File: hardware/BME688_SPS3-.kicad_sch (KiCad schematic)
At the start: 10 parts, among them U59 USBLC6-2P6, U6 BME688

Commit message: Debugging LED added
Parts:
- R3, R4, R5, R6: footprint Resistor_SMD:R_0603_1608Metric -> Resistor_SMD:R_0805_2012Metric
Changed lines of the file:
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@@
 			)
 		)
-		(property "Footprint" "Resistor_SMD:R_0603_1608Metric"
+		(property "Footprint" "Resistor_SMD:R_0805_2012Metric"
 			(at 172.212 104.14 90)
 			(effects
@@
 			)
 		)
-		(property "Footprint" "Resistor_SMD:R_0603_1608Metric"
+		(property "Footprint" "Resistor_SMD:R_0805_2012Metric"
 			(at 181.102 104.14 90)
 			(effects
@@
 			)
 		)
-		(property "Footprint" "Resistor_SMD:R_0603_1608Metric"
+		(property "Footprint" "Resistor_SMD:R_0805_2012Metric"
 			(at 84.328 101.6 90)
 			(effects
@@
 			)
 		)
-		(property "Footprint" "Resistor_SMD:R_0603_1608Metric"
+		(property "Footprint" "Resistor_SMD:R_0805_2012Metric"
 			(at 120.142 95.25 90)
 			(effects

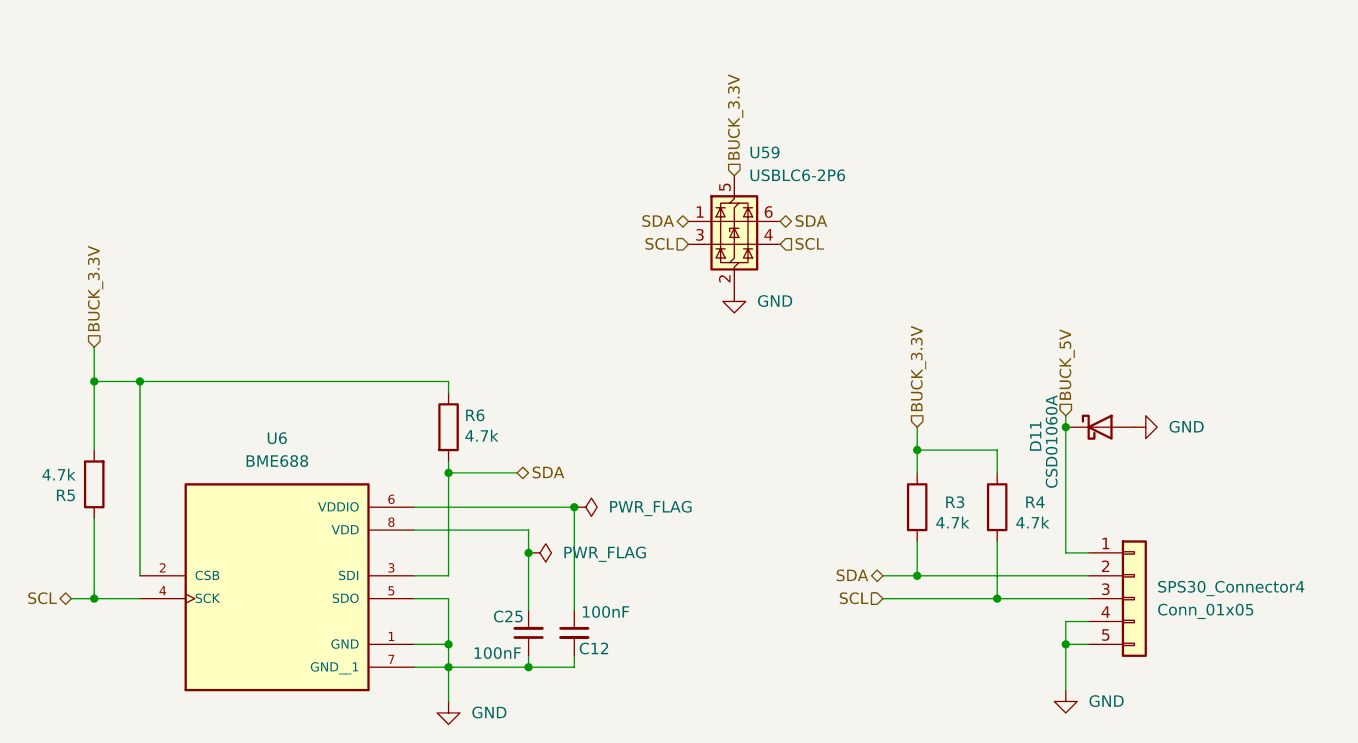
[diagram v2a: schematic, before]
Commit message: Unified I2C pull-ups to MCU page
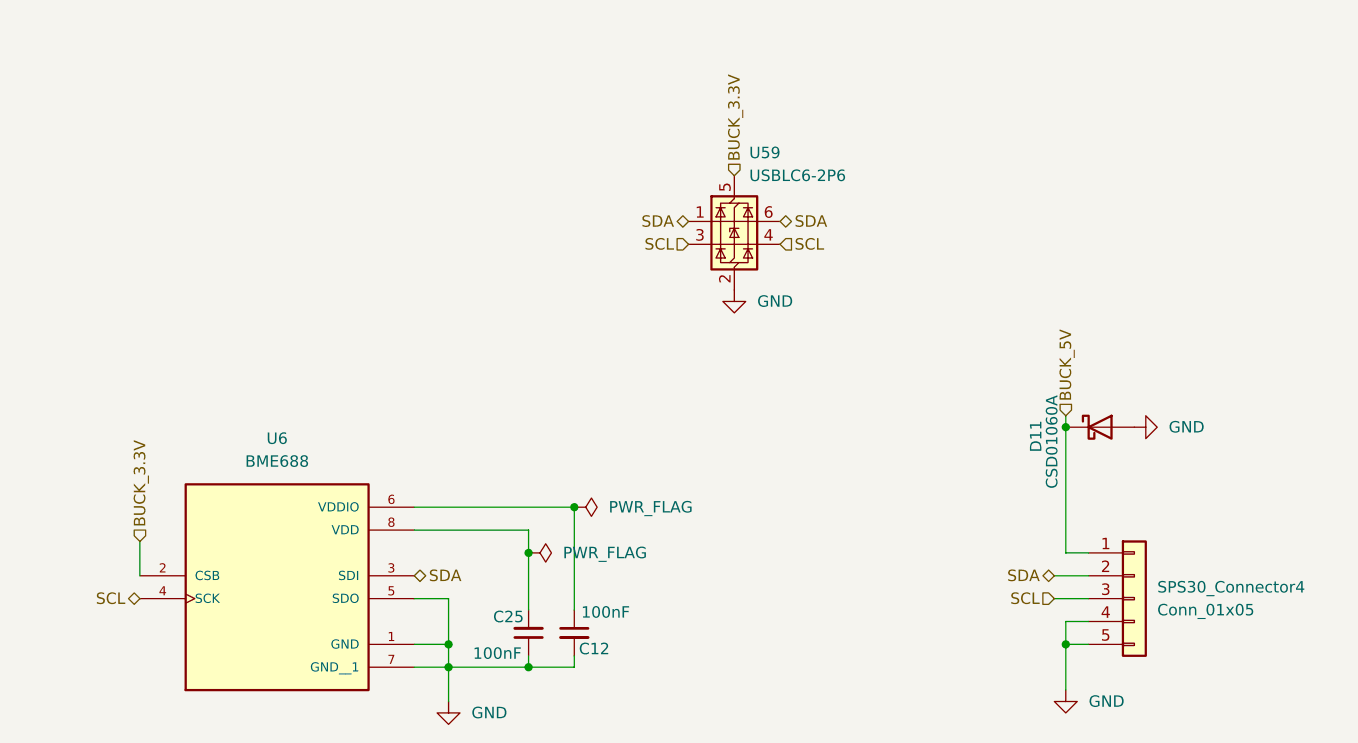
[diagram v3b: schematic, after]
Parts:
- removed R3, R4, R5, R6: 4.7k, Resistor_SMD:R_0805_2012Metric, symbol Device:R

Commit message: Fixed MCU JTAG/Reordered pages
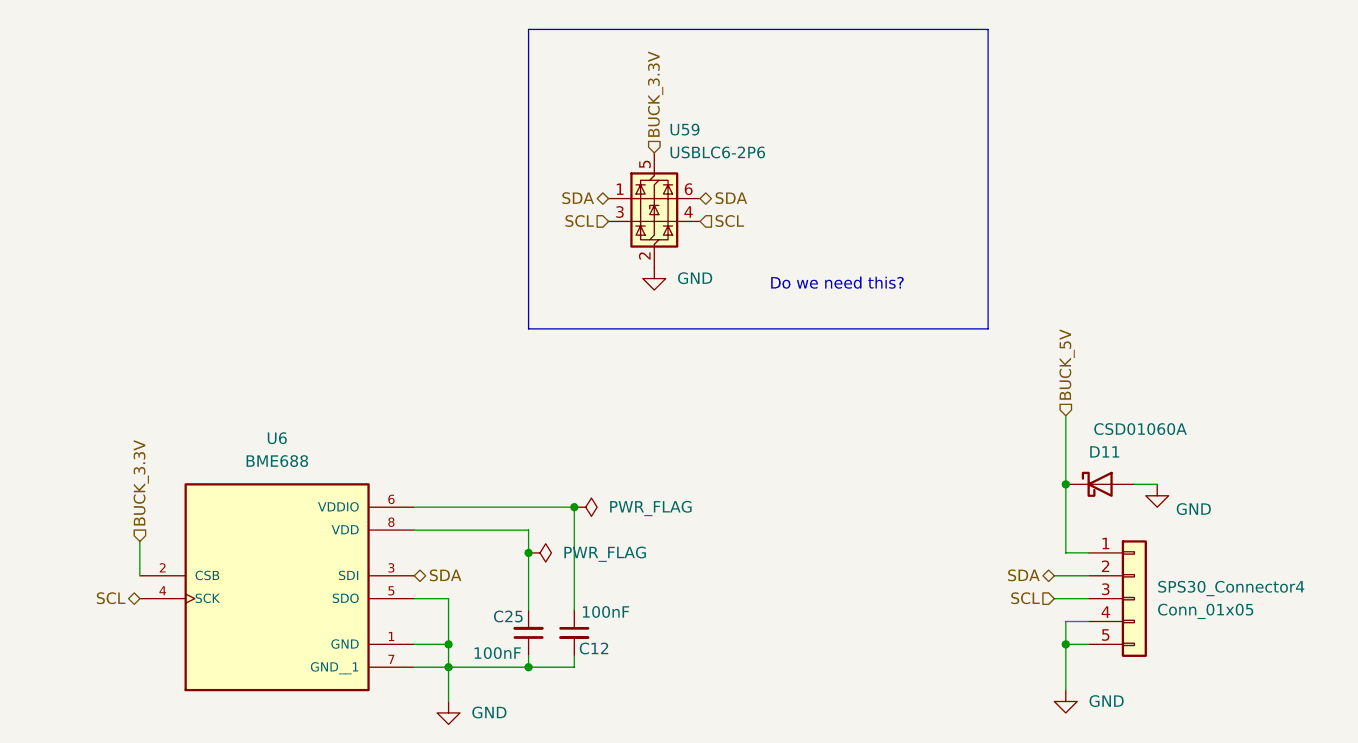
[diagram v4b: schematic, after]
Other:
- note added: "Do we need this?"
- moved on the sheet: D11, U59
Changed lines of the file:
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@@
 	(generator_version "9.0")
 	(paper "A4")
+	(rectangle
+		(start 130.81 51.054)
+		(end 181.864 84.328)
+		(stroke
+			(width 0)
+			(type default)
+		)
+		(fill
+			(type none)
+		)
+	)
+	(text "Do we need this?"
+		(exclude_from_sim no)
+		(at 165.1 79.502 0)
+		(effects
+			(font
+				(size 1.27 1.27)
+				(color 255 0 0 1)
+			)
+		)
+	)
 	(junction
 		(at 135.89 104.14)
@@
 	)
 	(junction
-		(at 190.5 95.25)
-		(diameter 0)
-		(color 0 0 0 0)
-	)
-	(junction
 		(at 121.92 121.92)
 		(diameter 0)
@@
 	)
 	(junction
+		(at 190.5 101.6)
+		(diameter 0)
+		(color 0 0 0 0)
+	)
+	(junction
 		(at 130.81 109.22)
 		(diameter 0)
@@
 	(wire
 		(pts
+			(xy 198.12 101.6) (xy 200.66 101.6)
+		)
+		(stroke
+			(width 0)
+			(type default)
+		)
+	)
+	(wire
+		(pts
 			(xy 135.89 120.65) (xy 135.89 121.92)
 		)
@@
 	(wire
 		(pts
-			(xy 190.5 93.98) (xy 190.5 95.25)
-		)
-		(stroke
-			(width 0)
-			(type default)
-		)
-	)
-	(wire
-		(pts
 			(xy 190.5 116.84) (xy 190.5 119.38)
 		)
@@
 	(wire
 		(pts
+			(xy 190.5 93.98) (xy 190.5 101.6)
+		)
+		(stroke
+			(width 0)
+			(type default)
+		)
+	)
+	(wire
+		(pts
 			(xy 118.11 114.3) (xy 121.92 114.3)
 		)
@@
 	(wire
 		(pts
-			(xy 190.5 95.25) (xy 190.5 109.22)
-		)
-		(stroke
-			(width 0)
-			(type default)
-		)
-	)
-	(wire
-		(pts
 			(xy 189.23 114.3) (xy 193.04 114.3)
 		)
@@
 		(pts
 			(xy 118.11 121.92) (xy 121.92 121.92)
+		)
+		(stroke
+			(width 0)
+			(type default)
+		)
+	)
+	(wire
+		(pts
+			(xy 190.5 101.6) (xy 190.5 109.22)
 		)
 		(stroke
@@
 	(hierarchical_label "SDA"
 		(shape bidirectional)
-		(at 148.59 72.39 180)
+		(at 139.7 69.85 180)
 		(effects
 			(font
@@
 	(hierarchical_label "BUCK_3.3V"
 		(shape input)
-		(at 153.67 67.31 90)
+		(at 144.78 64.77 90)
 		(effects
 			(font
@@
 	(hierarchical_label "SCL"
 		(shape input)
-		(at 148.59 74.93 180)
+		(at 139.7 72.39 180)
 		(effects
 			(font
@@
 	(hierarchical_label "SDA"
 		(shape bidirectional)
-		(at 158.75 72.39 0)
+		(at 149.86 69.85 0)
 		(effects
 			(font
@@
 	(hierarchical_label "SCL"
 		(shape input)
-		(at 158.75 74.93 0)
+		(at 149.86 72.39 0)
 		(effects
 			(font
@@
 	(symbol
 		(lib_id "Power_Protection:USBLC6-2P6")
-		(at 153.67 72.39 0)
+		(at 144.78 69.85 0)
 		(unit 1)
 		(exclude_from_sim no)
@@
 		(fields_autoplaced yes)
 		(property "Reference" "U59"
-			(at 155.3211 64.77 0)
+			(at 146.4311 62.23 0)
 			(effects
 				(font
@@
 		)
 		(property "Value" "USBLC6-2P6"
-			(at 155.3211 67.31 0)
+			(at 146.4311 64.77 0)
 			(effects
 				(font
@@
 		)
 		(property "Footprint" "Package_TO_SOT_SMD:SOT-666"
-			(at 154.686 79.121 0)
+			(at 145.796 76.581 0)
 			(effects
 				(font
@@
 		)
 		(property "Datasheet" "https://www.st.com/resource/en/datasheet/usblc6-2.pdf"
-			(at 154.686 81.026 0)
+			(at 145.796 78.486 0)
 			(effects
 				(font
@@
 		)
 		(property "Description" "Very low capacitance ESD protection diode, 2 data-line, SOT-666"
-			(at 153.67 72.39 0)
+			(at 144.78 69.85 0)
 			(effects
 				(font
@@
 	(symbol
 		(lib_id "Diode:CSD01060A")
-		(at 194.31 95.25 0)
+		(at 194.31 101.6 0)
 		(unit 1)
 		(exclude_from_sim no)
@@
 		(dnp no)
 		(property "Reference" "D11"
-			(at 187.198 94.488 90)
+			(at 196.596 98.044 0)
 			(effects
 				(font
@@
 		)
 		(property "Value" "CSD01060A"
-			(at 188.976 91.694 90)
+			(at 203.962 95.504 0)
 			(effects
 				(font
@@
 		)
 		(property "Footprint" "Package_TO_SOT_THT:TO-220-2_Vertical"
-			(at 194.31 99.695 0)
+			(at 194.31 106.045 0)
 			(effects
 				(font
@@
 		)
 		(property "Datasheet" "https://www.wolfspeed.com/media/downloads/87/CSD01060.pdf"
-			(at 194.31 95.25 0)
+			(at 194.31 101.6 0)
 			(effects
 				(font
@@
 		)
 		(property "Description" "600V, 1A, SiC Schottky Diode, TO-220"
-			(at 194.31 95.25 0)
+			(at 194.31 101.6 0)
 			(effects
 				(font
@@
 	(symbol
 		(lib_id "power:GND")
-		(at 198.12 95.25 90)
+		(at 200.66 101.6 0)
 		(unit 1)
 		(exclude_from_sim no)
@@
 		(on_board yes)
 		(dnp no)
-		(fields_autoplaced yes)
 		(property "Reference" "#PWR0116"
-			(at 204.47 95.25 0)
+			(at 200.66 107.95 0)
 			(effects
 				(font
@@
 		)
 		(property "Value" "GND"
-			(at 201.93 95.2499 90)
-			(effects
-				(font
-					(size 1.27 1.27)
-				)
-				(justify right)
+			(at 204.724 104.394 0)
+			(effects
+				(font
+					(size 1.27 1.27)
+				)
 			)
 		)
 		(property "Footprint" ""
-			(at 198.12 95.25 0)
+			(at 200.66 101.6 0)
 			(effects
 				(font
@@
 		)
 		(property "Datasheet" ""
-			(at 198.12 95.25 0)
+			(at 200.66 101.6 0)
 			(effects
 				(font
@@
 		)
 		(property "Description" "Power symbol creates a global label with name \"GND\" , ground"
-			(at 198.12 95.25 0)
+			(at 200.66 101.6 0)
 			(effects
 				(font
@@
 	(symbol
 		(lib_id "power:GND")
-		(at 153.67 80.01 0)
+		(at 144.78 77.47 0)
 		(unit 1)
 		(exclude_from_sim no)
@@
 		(fields_autoplaced yes)
 		(property "Reference" "#PWR0114"
-			(at 153.67 86.36 0)
+			(at 144.78 83.82 0)
 			(effects
 				(font
@@
 		)
 		(property "Value" "GND"
-			(at 156.21 81.2799 0)
+			(at 147.32 78.7399 0)
 			(effects
 				(font
@@
 		)
 		(property "Footprint" ""
-			(at 153.67 80.01 0)
+			(at 144.78 77.47 0)
 			(effects
 				(font
@@
 		)
 		(property "Datasheet" ""
-			(at 153.67 80.01 0)
+			(at 144.78 77.47 0)
 			(effects
 				(font
@@
 		)
 		(property "Description" "Power symbol creates a global label with name \"GND\" , ground"
-			(at 153.67 80.01 0)
-			(effects
-				(font
+			(at 144.78 77.47 0)
+			(effects
+				(font

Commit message: Replaced 3.3V symbol
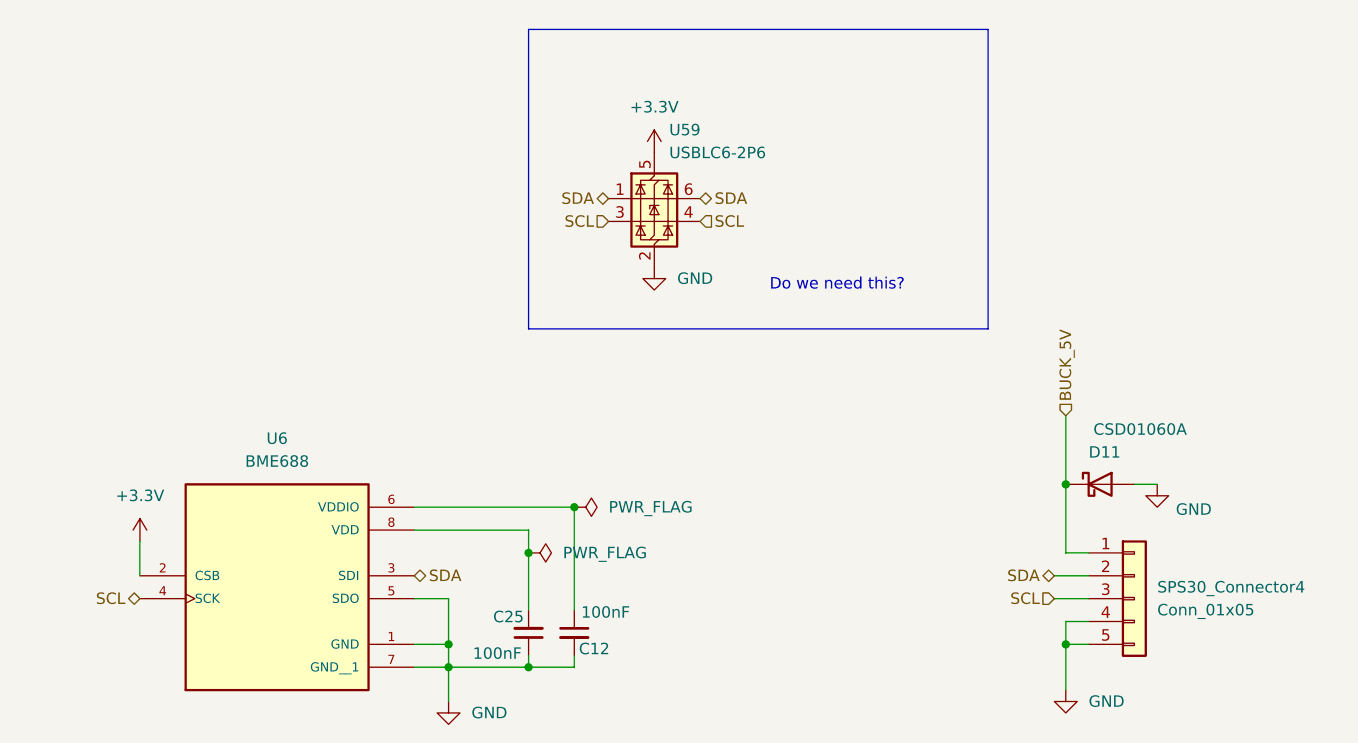
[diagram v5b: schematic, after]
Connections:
- net BUCK_3.3V renamed +3.3V
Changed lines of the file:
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@@
-		)
-	)
-	(hierarchical_label "BUCK_3.3V"
-		(shape input)
-		(at 144.78 64.77 90)
-		(effects
-			(font
-				(size 1.27 1.27)
-			)
-			(justify left)
 		)
 	)
@@
 		(shape bidirectional)
 		(at 149.86 69.85 0)
-		(effects
-			(font
-				(size 1.27 1.27)
-			)
-			(justify left)
-		)
-	)
-	(hierarchical_label "BUCK_3.3V"
-		(shape input)
-		(at 87.63 107.95 90)
 		(effects
 			(font
@@
 	)
 	(symbol
+		(lib_id "power:+3.3V")
+		(at 87.63 107.95 0)
+		(unit 1)
+		(exclude_from_sim no)
+		(in_bom yes)
+		(on_board yes)
+		(dnp no)
+		(fields_autoplaced yes)
+		(property "Reference" "#PWR077"
+			(at 87.63 111.76 0)
+			(effects
+				(font
+					(size 1.27 1.27)
+				)
+				(hide yes)
+			)
+		)
+		(property "Value" "+3.3V"
+			(at 87.63 102.87 0)
+			(effects
+				(font
+					(size 1.27 1.27)
+				)
+			)
+		)
+		(property "Footprint" ""
+			(at 87.63 107.95 0)
+			(effects
+				(font
+					(size 1.27 1.27)
+				)
+				(hide yes)
+			)
+		)
+		(property "Datasheet" ""
+			(at 87.63 107.95 0)
+			(effects
+				(font
+					(size 1.27 1.27)
+				)
+				(hide yes)
+			)
+		)
+		(property "Description" "Power symbol creates a global label with name \"+3.3V\""
+			(at 87.63 107.95 0)
+			(effects
+				(font
+					(size 1.27 1.27)
+				)
+				(hide yes)
+			)
+		)
+		(pin "1"
+		)
+		(instances
+			(project "Senior_Design"
+				(path "/8f5928e8-0fc1-4443-a20f-3bfeb956761e/140ad835-eaa4-4a8c-a4e7-0525bbf22a2e"
+					(reference "#PWR077")
+					(unit 1)
+				)
+			)
+		)
+	)
+	(symbol
 		(lib_id "Device:C_Small")
 		(at 135.89 118.11 0)
@@
 					(unit 1)
 				)
+			)
+		)
+	)
+	(symbol
+		(lib_id "power:+3.3V")
+		(at 144.78 64.77 0)
+		(unit 1)
+		(exclude_from_sim no)
+		(in_bom yes)
+		(on_board yes)
+		(dnp no)
+		(fields_autoplaced yes)
+		(property "Reference" "#PWR078"
+			(at 144.78 68.58 0)
+			(effects
+				(font
+					(size 1.27 1.27)
+				)
+				(hide yes)
+			)
+		)
+		(property "Value" "+3.3V"
+			(at 144.78 59.69 0)
+			(effects
+				(font
+					(size 1.27 1.27)
+				)
+			)
+		)
+		(property "Footprint" ""
+			(at 144.78 64.77 0)
+			(effects
+				(font
+					(size 1.27 1.27)
+				)
+				(hide yes)
+			)
+		)
+		(property "Datasheet" ""
+			(at 144.78 64.77 0)
+			(effects
+				(font
+					(size 1.27 1.27)
+				)
+				(hide yes)
+			)
+		)
+		(property "Description" "Power symbol creates a global label with name \"+3.3V\""
+			(at 144.78 64.77 0)
+			(effects
+				(font
+					(size 1.27 1.27)
+				)
+				(hide yes)
+			)
+		)
+		(pin "1"
+		)
+		(instances
+			(project "Senior_Design"
+				(path "/8f5928e8-0fc1-4443-a20f-3bfeb956761e/140ad835-eaa4-4a8c-a4e7-0525bbf22a2e"
+					(reference "#PWR078")
+					(unit 1)
+				)

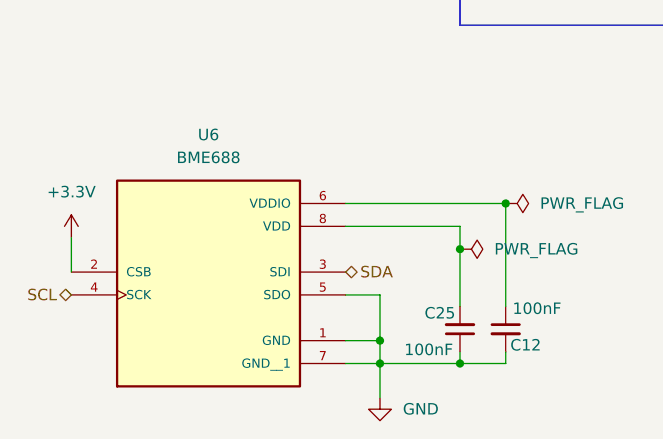
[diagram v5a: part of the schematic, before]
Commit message: updated major symbol and footprints
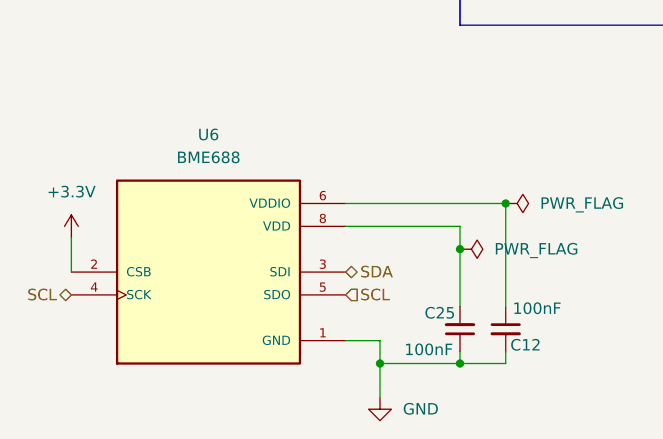
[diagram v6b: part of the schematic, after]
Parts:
- U6: footprint Custom_Parts:IC_BME688 -> pyronet_footprints:IC_BME688; symbol BME688:BME688 -> pyronet_symbols:BME688; Availability (none) -> In Stock; Check_prices (none) -> https://www.snapeda.com/parts/BME688/Bosch/view-part/?ref=e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; Description_1 (none) -> Gas sensor measuring relative humidity, barometric pressure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; MF (none) -> Bosch Sensortec; MP (none) -> BME688; Package (none) -> None; Price (none) -> None; Purchase-URL (none) -> https://www.snapeda.com/api/url_track_click_mouser/?unipart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; SnapEDA_Link (none) -> https://www.snapeda.com/parts/BME688/Bosch/view-part/?ref=s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
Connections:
- net GND: no longer U6.5 (SDO)
- net SCL: now also U6.5 (SDO)
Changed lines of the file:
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@@
-	)
-	(junction
-		(at 121.92 119.38)
-		(diameter 0)
-		(color 0 0 0 0)
 	)
 	(junction
@@
 	(wire
 		(pts
-			(xy 118.11 114.3) (xy 121.92 114.3)
-		)
-		(stroke
-			(width 0)
-			(type default)
-		)
-	)
-	(wire
-		(pts
 			(xy 121.92 121.92) (xy 121.92 125.73)
 		)
@@
 		(pts
 			(xy 118.11 106.68) (xy 130.81 106.68)
-		)
-		(stroke
-			(width 0)
-			(type default)
-		)
-	)
-	(wire
-		(pts
-			(xy 121.92 114.3) (xy 121.92 119.38)
-		)
-		(stroke
-			(width 0)
-			(type default)
-		)
-	)
-	(wire
-		(pts
-			(xy 118.11 121.92) (xy 121.92 121.92)
 		)
 		(stroke
@@
 		(shape bidirectional)
 		(at 118.11 111.76 0)
+		(effects
+			(font
+				(size 1.27 1.27)
+			)
+			(justify left)
+		)
+	)
+	(hierarchical_label "SCL"
+		(shape input)
+		(at 118.11 114.3 0)
 		(effects
 			(font
@@
 	)
 	(symbol
-		(lib_id "BME688:BME688")
+		(lib_id "pyronet_symbols:BME688")
 		(at 102.87 111.76 0)
 		(unit 1)
@@
 			)
 		)
-		(property "Footprint" "Custom_Parts:IC_BME688"
+		(property "Footprint" "pyronet_footprints:IC_BME688"
 			(at 102.87 111.76 0)
 			(effects
@@
 			(at 102.87 111.76 0)
 			(effects
+				(font
+					(size 1.27 1.27)
+				)
+				(justify bottom)
+				(hide yes)
+			)
+		)
+		(property "MF" "Bosch Sensortec"
+			(at 102.87 111.76 0)
+			(effects
+				(font
+					(size 1.27 1.27)
+				)
+				(justify bottom)
+				(hide yes)
+			)
+		)
+		(property "Package" "None"
+			(at 102.87 111.76 0)
+			(effects
+				(font
+					(size 1.27 1.27)
+				)
+				(justify bottom)
+				(hide yes)
+			)
+		)
+		(property "Price" "None"
+			(at 102.87 111.76 0)
+			(effects
+				(font
+					(size 1.27 1.27)
+				)
+				(justify bottom)
+				(hide yes)
+			)
+		)
+		(property "Check_prices" "https://www.snapeda.com/parts/BME688/Bosch/view-part/?ref=eda"
+			(at 102.87 111.76 0)
+			(effects
+				(font
+					(size 1.27 1.27)
+				)
+				(justify bottom)
+				(hide yes)
+			)
+		)
+		(property "SnapEDA_Link" "https://www.snapeda.com/parts/BME688/Bosch/view-part/?ref=snap"
+			(at 102.87 111.76 0)
+			(effects
+				(font
+					(size 1.27 1.27)
+				)
+				(justify bottom)
+				(hide yes)
+			)
+		)
+		(property "MP" "BME688"
+			(at 102.87 111.76 0)
+			(effects
+				(font
+					(size 1.27 1.27)
+				)
+				(justify bottom)
+				(hide yes)
+			)
+		)
+		(property "Purchase-URL" "https://www.snapeda.com/api/url_track_click_mouser/?unipart_id=5697293&manufacturer=Bosch Sensortec&part_name=BME688&search_term=bme688"
+			(at 102.87 111.76 0)
+			(effects
+				(font
+					(size 1.27 1.27)
+				)
+				(justify bottom)
+				(hide yes)
+			)
+		)
+		(property "Description_1" "Gas sensor measuring relative humidity, barometric pressure, ambient temperature and gas (VOC)"
+			(at 102.87 111.76 0)
+			(effects
+				(font
+					(size 1.27 1.27)
+				)
+				(justify bottom)
+				(hide yes)
+			)
+		)
+		(property "Availability" "In Stock"
+			(at 102.87 111.76 0)
+			(effects
